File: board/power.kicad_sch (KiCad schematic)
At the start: 2 parts, among them U1 TPS25730D

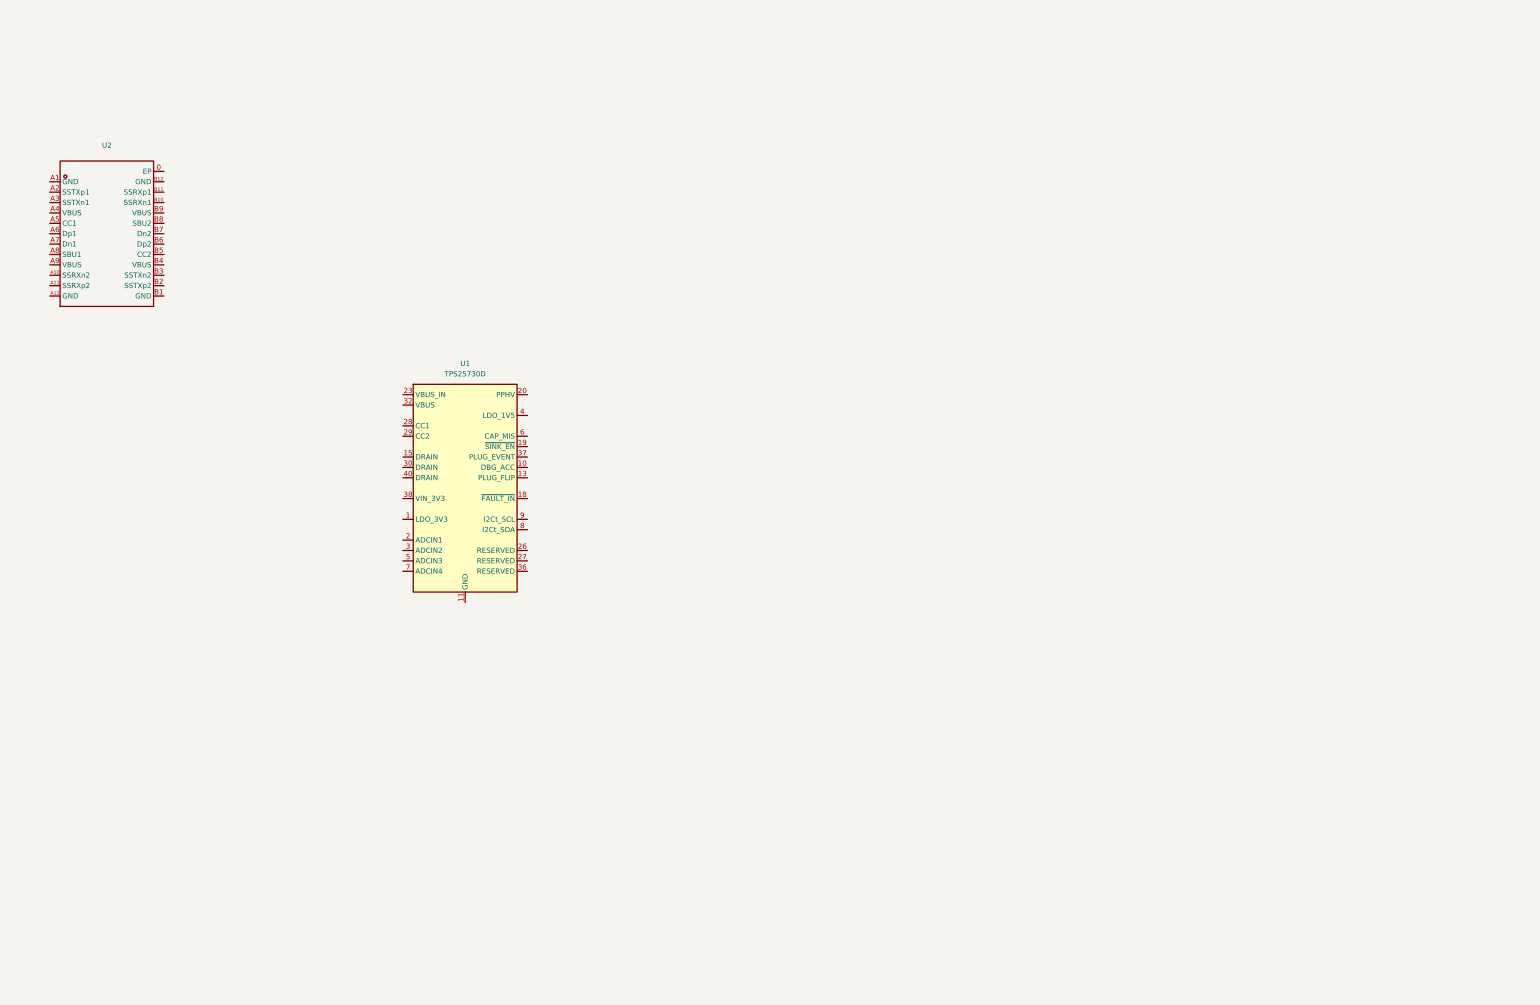
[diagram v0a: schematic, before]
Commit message: Finished everything except assigning footprints for passives
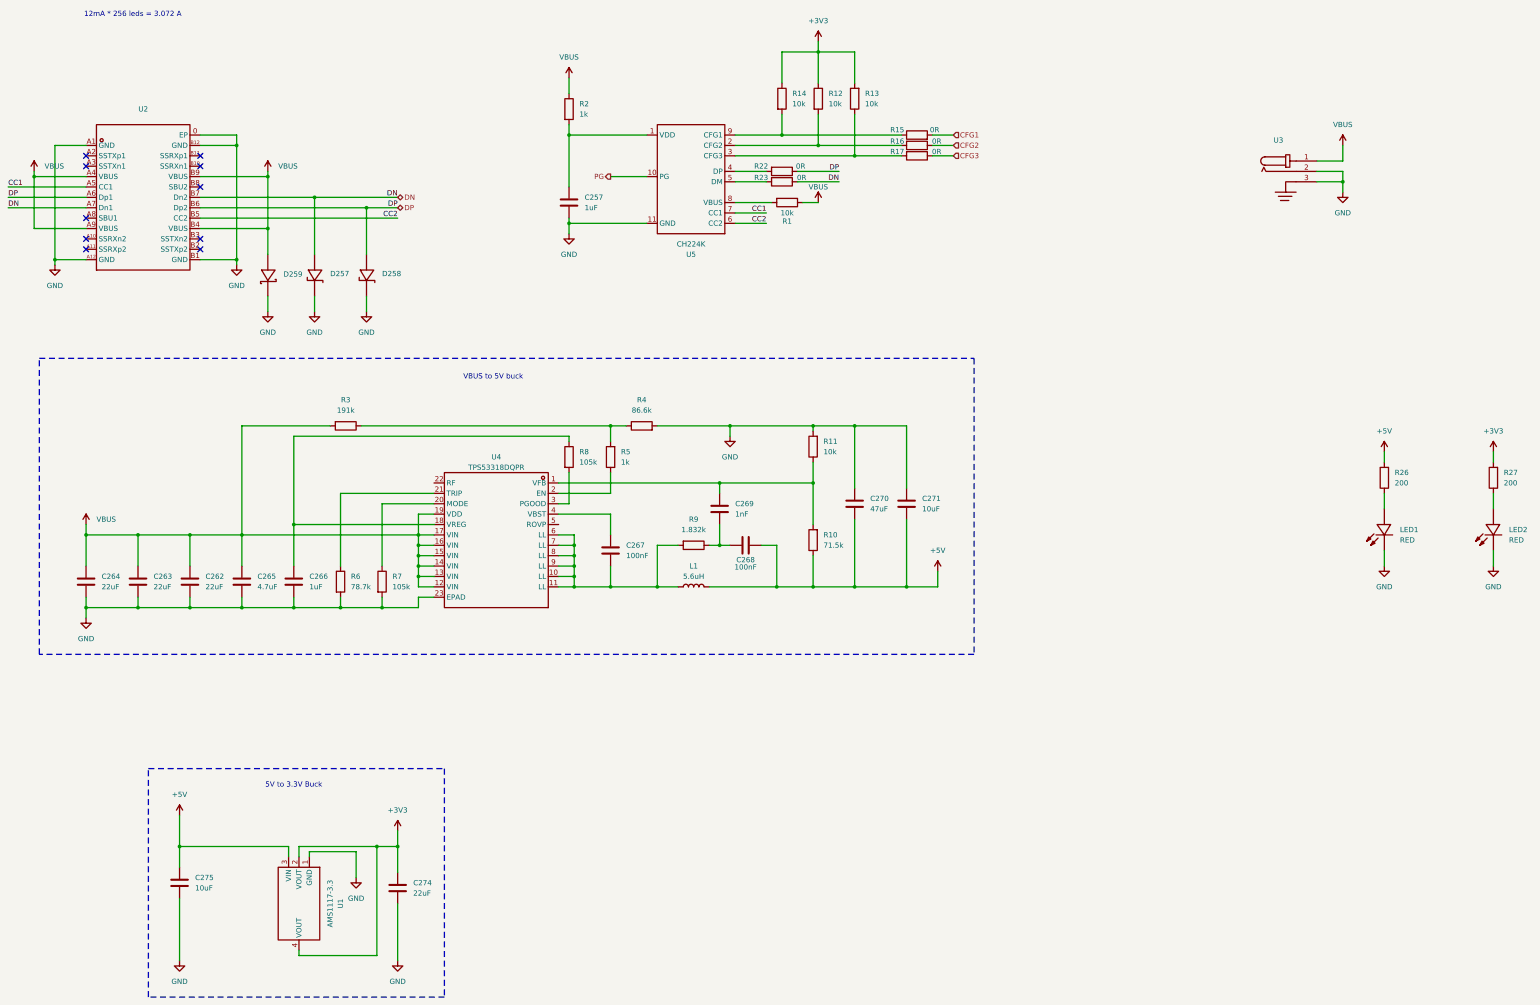
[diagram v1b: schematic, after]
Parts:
- removed U1: TPS25730D, Package_DFN_QFN:Texas_REF0038A_WQFN-38-2EP_6x4mm_P0.4, symbol Interface_USB:TPS25730D
- added C257, C266: 1uF, symbol Device:C
- added C262, C263, C264, C274: 22uF, symbol Device:C
- added C265: 4.7uF, symbol Device:C
- added C267, C268: 100nF, symbol Device:C
- added C269: 1nF, Capacitor_SMD:C_0402_1005Metric_Pad0.74x0.62mm_HandSolder, symbol Device:C
- added C270: 47uF, symbol Device:C
- added C271, C275: 10uF, Capacitor_SMD:C_0402_1005Metric_Pad0.74x0.62mm_HandSolder, symbol Device:C
- added D257, D258: ~, led_matrix:SOD-523F_L1.2-W0.8-LS1.7-RD, symbol led_matrix:ESD5Z5.0T1G
- added D259: ~, led_matrix:SOD-123_L2.7-W1.6-LS3.7-RD, symbol led_matrix:SMF22A
- added L1: 5.6uH, symbol Device:L
- added LED1, LED2: RED, led_matrix:LED0603-RD, symbol led_matrix:KT-0603R
- added R1, R11, R12, R13, R14: 10k, symbol Device:R
- added R10: 71.5k, symbol Device:R
- added R15, R16, R17, R22, R23: 0R, symbol Device:R
- added R2, R5: 1k, symbol Device:R
- added R26, R27: 200, symbol Device:R
- added R3: 191k, symbol Device:R
- added R4: 86.6k, symbol Device:R
- added R6: 78.7k, symbol Device:R
- added R7, R8: 105k, symbol Device:R
- added R9: 1.832k, symbol Device:R
- added U1: AMS1117-3.3, led_matrix:SOT-223-3_L6.5-W3.4-P2.30-LS7.0-BR, symbol led_matrix:AMS1117-3.3
- added U3: ~, led_matrix:DC-IN-TH_HX-DC007B-2.5, symbol led_matrix:HX DC007B-2.5
- added U4: TPS53318DQPR, led_matrix:LSON-CLIP-22_L6.0-W5.0-P0.50-BL-EP, symbol led_matrix:TPS53318DQPR
- added U5: CH224K, led_matrix:ESSOP-10_L4.9-W3.9-P1.0-LS6.0-TL-EP, symbol led_matrix:CH224K
- U2: footprint ProLib_pcs_2025-07-06:TYPE-C-USB-SMD_QCHT-143 -> led_matrix:TYPE-C-USB-SMD_QCHT-143
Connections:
- net GND: now reaches U2.0 (EP)
- net GND: now also U2.A1 (GND), U2.A12 (GND), U2.B1 (GND), U2.B12 (GND), C257.2, C262.2, C263.2, C264.2, C265.2, C266.2, C270.1, C271.1, C274.2, C275.2, D257.1 (C), D258.1 (C), D259.1 (K), LED1.1 (K), LED2.1 (K), R11.2, R4.2, R6.2, R7.2, U1.1 (GND), U3.2, U3.3, U4.23 (EPAD), U5.11 (GND)
- net VBUS: now reaches U2.A4 (VBUS)
- net VBUS: now also U2.A9 (VBUS), U2.B4 (VBUS), U2.B9 (VBUS), C262.1, C263.1, C264.1, C265.1, D259.2 (A), R1.1, R2.1, R3.2, U3.1, U4.12 (VIN), U4.13 (VIN), U4.14 (VIN), U4.15 (VIN), U4.16 (VIN), U4.17 (VIN), U4.19 (VDD)
- net CC1: now reaches U2.A5 (CC1)
- net CC1: now also U5.7 (CC1)
- net DP: now reaches U2.A6 (Dp1)
- net DP: now also U2.B6 (Dp2), D258.2 (A), R22.1
- net DN: now reaches U2.A7 (Dn1)
- net DN: now also U2.B7 (Dn2), D257.2 (A), R23.1
- net CC2: now reaches U2.B5 (CC2)
- net CC2: now also U5.6 (CC2)
- new net: C257.1, R2.2, U5.1 (VDD)
- new net: R13.1, R17.2, U5.3 (CFG3)
- new net: C268.1, C269.1, R9.1
- new net: C267.1, L1.1, R9.2, U4.10 (LL), U4.11 (LL), U4.6 (LL), U4.7 (LL), U4.8 (LL), U4.9 (LL)
- new net: R22.2, U5.4 (DP)
- new net: R3.1, R4.1, R5.2
- new net: C269.2, R10.2, R11.1, U4.1 (VFB)
- new net: R1.2, U5.8 (VBUS)
- new net: R12.2, R16.2, U5.2 (CFG2)
- new net: R23.2, U5.5 (DM)
- new net: R14.2, R15.1, U5.9 (CFG1)
- new net: R7.1, U4.20 (MODE)
- new net: C266.1, R8.1, U4.18 (VREG)
- new net: R8.2, U4.3 (PGOOD)
- new net: R5.1, U4.2 (EN)
- new net: R6.1, U4.21 (TRIP)
- new net: C267.2, U4.4 (VBST)
- new net: LED2.2 (A), R27.1
- new net: LED1.2 (A), R26.1
- new net +3V3: C274.1, R12.1, R13.2, R14.1, R27.2, U1.2 (VOUT), U1.4 (VOUT)
- new net +5V: C268.2, C270.2, C271.2, C275.1, L1.2, R10.1, R26.2, U1.3 (VIN)
- new net CFG1: R15.2
- new net CFG2: R16.1
- new net CFG3: R17.1
- new net PG: U5.10 (PG)
- no-connect marks 0 -> 10
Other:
- note added: "12mA * 256 leds = 3.072 A"
- note added: "5V to 3.3V Buck"
- note added: "VBUS to 5V buck"

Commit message: Added footprints for everything except buck inductor and resistor
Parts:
- C257, C266: footprint (none) -> Capacitor_SMD:C_0402_1005Metric_Pad0.74x0.62mm_HandSolder; LCSC Part Name (none) -> C52923
- C262, C263, C264, C274: footprint (none) -> Capacitor_SMD:C_0805_2012Metric_Pad1.18x1.45mm_HandSolder; LCSC Part Name (none) -> C45783
- C265: footprint (none) -> Capacitor_SMD:C_0603_1608Metric_Pad1.08x0.95mm_HandSolder; LCSC Part Name (none) -> C19666
- C267, C268: footprint (none) -> Capacitor_SMD:C_0402_1005Metric_Pad0.74x0.62mm_HandSolder; LCSC Part Name (none) -> C307331
- C270: footprint (none) -> Capacitor_SMD:C_1206_3216Metric_Pad1.33x1.80mm_HandSolder; LCSC Part Name (none) -> C96123
- R1, R11, R12, R13, R14: footprint (none) -> Resistor_SMD:R_0603_1608Metric_Pad0.98x0.95mm_HandSolder; LCSC Part Name (none) -> C25804
- R10: footprint (none) -> Resistor_SMD:R_0603_1608Metric_Pad0.98x0.95mm_HandSolder; LCSC Part Name (none) -> C304779
- R2, R5: footprint (none) -> Resistor_SMD:R_0402_1005Metric_Pad0.72x0.64mm_HandSolder; LCSC Part Name (none) -> C11702
- R26, R27: footprint (none) -> Resistor_SMD:R_0603_1608Metric_Pad0.98x0.95mm_HandSolder; LCSC Part Name (none) -> C8218
- R3: footprint (none) -> Resistor_SMD:R_0603_1608Metric_Pad0.98x0.95mm_HandSolder; LCSC Part Name (none) -> C2974031
- R4: footprint (none) -> Resistor_SMD:R_0603_1608Metric_Pad0.98x0.95mm_HandSolder; LCSC Part Name (none) -> C304789
- R6: footprint (none) -> Resistor_SMD:R_0603_1608Metric_Pad0.98x0.95mm_HandSolder; LCSC Part Name (none) -> C304782
- R7, R8: footprint (none) -> Resistor_SMD:R_0603_1608Metric_Pad0.98x0.95mm_HandSolder; LCSC Part Name (none) -> C3016070

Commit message: Started layout
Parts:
- removed C270: 47uF, Capacitor_SMD:C_1206_3216Metric_Pad1.33x1.80mm_HandSolder, symbol Device:C
- removed C271: 10uF, Capacitor_SMD:C_0402_1005Metric_Pad0.74x0.62mm_HandSolder, symbol Device:C
- removed D257, D258: ~, led_matrix:SOD-523F_L1.2-W0.8-LS1.7-RD, symbol led_matrix:ESD5Z5.0T1G
- removed D259: ~, led_matrix:SOD-123_L2.7-W1.6-LS3.7-RD, symbol led_matrix:SMF22A
- removed L1: 5.6uH, symbol Device:L
- removed U2: ~, led_matrix:TYPE-C-USB-SMD_QCHT-143, symbol led_matrix:TYPE-C 24P QCHT 143
- removed U3: ~, led_matrix:DC-IN-TH_HX-DC007B-2.5, symbol led_matrix:HX DC007B-2.5
- added C270, C271: 1mF, led_matrix:CAP_EEFC_G_PAN-L, symbol led_matrix:EEE-FC1A102P
- added C276: 22uF, Capacitor_SMD:C_1206_3216Metric_Pad1.33x1.80mm_HandSolder, symbol Device:C
- added C277: 560uF, led_matrix:PCAP_SVP_F12_PAN-L, symbol led_matrix:10SVP560M
- added D257, D258: ~, led_matrix:SOD-523_L1.2-W0.8-LS1.6-BI, symbol led_matrix:LESD5D5.0CT1G
- added DC1: ~, led_matrix:DC-IN-TH_DC-005-5A-2.0-SMT, symbol led_matrix:DC-005-5A-2.5-SMT
- added L1: 4.7uH, led_matrix:IND_BOURNS_SRP1250-L, symbol led_matrix:SRP1250-4R7M
- added USB1: ~, led_matrix:USB-C-SMD_GT-USB-7047A, symbol led_matrix:GT-USB-7047A
- C262, C263, C264, C274: footprint Capacitor_SMD:C_0805_2012Metric_Pad1.18x1.45mm_HandSolder -> Capacitor_SMD:C_1206_3216Metric_Pad1.33x1.80mm_HandSolder; LCSC Part Name C45783 -> C12891
- C265: footprint Capacitor_SMD:C_0603_1608Metric_Pad1.08x0.95mm_HandSolder -> Capacitor_SMD:C_1206_3216Metric_Pad1.33x1.80mm_HandSolder; LCSC Part Name C19666 -> C29823
- C266: footprint Capacitor_SMD:C_0402_1005Metric_Pad0.74x0.62mm_HandSolder -> Capacitor_SMD:C_0805_2012Metric_Pad1.18x1.45mm_HandSolder; LCSC Part Name C52923 -> C28323
- C267, C268: footprint Capacitor_SMD:C_0402_1005Metric_Pad0.74x0.62mm_HandSolder -> Capacitor_SMD:C_0805_2012Metric_Pad1.18x1.45mm_HandSolder; LCSC Part Name C307331 -> C28233
- C269: footprint Capacitor_SMD:C_0402_1005Metric_Pad0.74x0.62mm_HandSolder -> Capacitor_SMD:C_0805_2012Metric_Pad1.18x1.45mm_HandSolder; LCSC Part Name C1523 -> C46653
- C275: footprint Capacitor_SMD:C_0402_1005Metric_Pad0.74x0.62mm_HandSolder -> Capacitor_SMD:C_0603_1608Metric_Pad1.08x0.95mm_HandSolder; LCSC Part Name (none) -> C19702
- LED1, LED2: LCSC Part Name 0603 红灯 高亮 -> C2286
- R15, R16, R17, R22, R23: footprint (none) -> Resistor_SMD:R_0603_1608Metric_Pad0.98x0.95mm_HandSolder; LCSC Part Name (none) -> C15402
- R3: value 191k -> 237k; LCSC Part Name C2974031 -> C22914
- R6: value 78.7k -> 124k; LCSC Part Name C304782 -> C22788
- R9: value 1.832k -> 1.82k; footprint (none) -> Resistor_SMD:R_0603_1608Metric_Pad0.98x0.95mm_HandSolder; LCSC Part Name (none) -> C25958
- U1: LCSC Part Name 输出3.3V 1A -> C6186
- U4: LCSC Part Name 高效8A或14A同步降压转换器 -> C179745
- U5: LCSC Part Name USBPD等多快充协议受电芯片CH224 -> C970725
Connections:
- net +5V: now also C270.1, C271.1, C277.1, L1.1
- net CC1: now also USB1.A5 (CC1)
- net CC2: now also USB1.B5 (CC2)
- net DN: now also D257.1, USB1.A7 (DN1), USB1.B7 (DN2)
- net DP: now also D258.1, USB1.A6 (DP1), USB1.B6 (DP2)
- net GND: now also C270.2, C271.2, C276.2, C277.2, D257.2, D258.2, DC1.2, USB1.1 (SHELL), USB1.2 (SHELL), USB1.3 (SHELL), USB1.4 (SHELL), USB1.A1B12 (GND), USB1.B1A12 (GND)
- net VBUS: now also C276.1, DC1.1, USB1.A4B9 (VBUS), USB1.B4A9 (VBUS)
- net at C267.1, R9.2, U4.10 (LL)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: now also L1.2
- no-connect marks 10 -> 2
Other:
- note added: "5V to 3.3V LDO"
- note added: "A resistor between the inductor and ground is necessary. The value of this resistor is ESR, and can be determined with equation 16. ESR = (L * f_sw) / 60 ESR = 0.0629 Ohms"
- note added: "Maximum current: 256 * 0.012A = 3.072A f_sw = 500kHz From datasheet, inductor ripple current should be from 0.25 to 0.5 times max output current. I have chosen 1/3 ripple current. Inductor ripple current can be used to find inductance value according to the following equation (14): L = (3/(I_out(max) * f_sw)) * (((V_in(max) - Vout) * Vout)/V_in(max)) L = 7.55uH The peak inductor current can be es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"
- note removed: "12mA * 256 leds = 3.072 A"
- note removed: "5V to 3.3V Buck"
- moved on the sheet: LED1, LED2, R26, R27

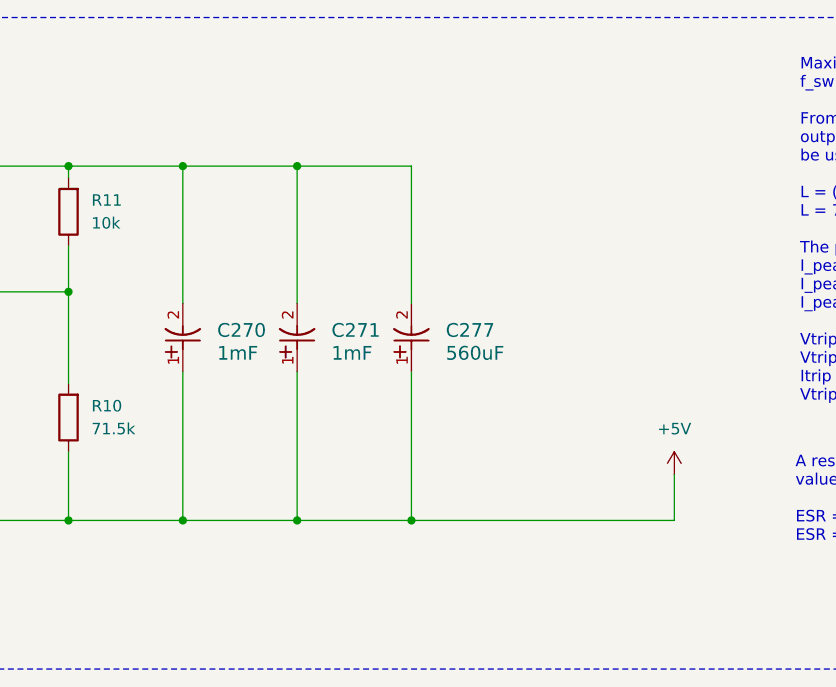
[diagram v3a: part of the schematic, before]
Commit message: Fixed buck output caps
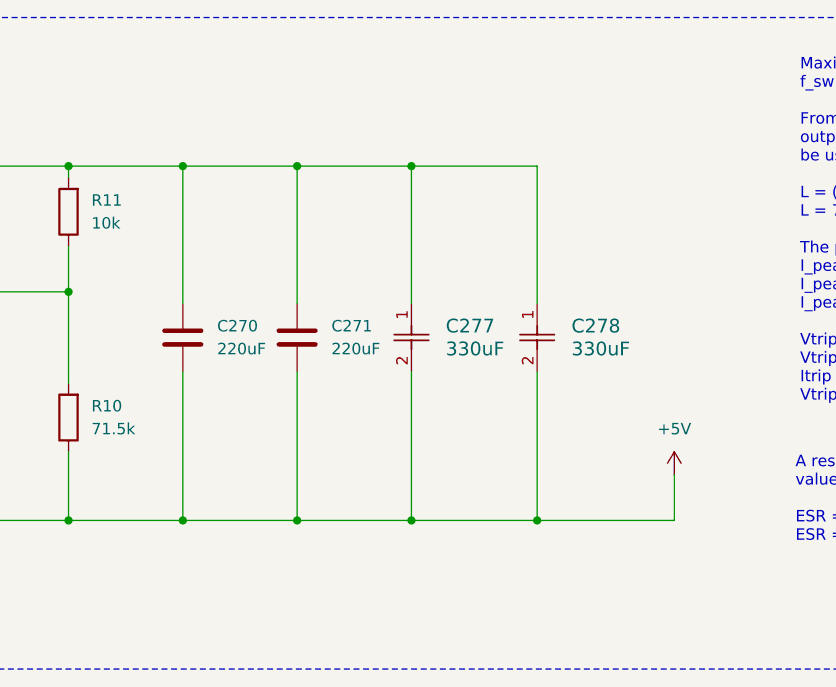
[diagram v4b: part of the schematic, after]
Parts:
- removed C270, C271: 1mF, led_matrix:CAP_EEFC_G_PAN-L, symbol led_matrix:EEE-FC1A102P
- removed C277: 560uF, led_matrix:PCAP_SVP_F12_PAN-L, symbol led_matrix:10SVP560M
- added C270, C271: 220uF, Capacitor_SMD:C_1206_3216Metric_Pad1.33x1.80mm_HandSolder, symbol Device:C
- added C277, C278: 330uF, led_matrix:CAP_293D_E_VIS-L, symbol led_matrix:293D337X9010E2TE3
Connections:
- net +5V: now also C270.2, C271.2, C277.2, C278.2
- net GND: now also C270.1, C271.1, C277.1, C278.1

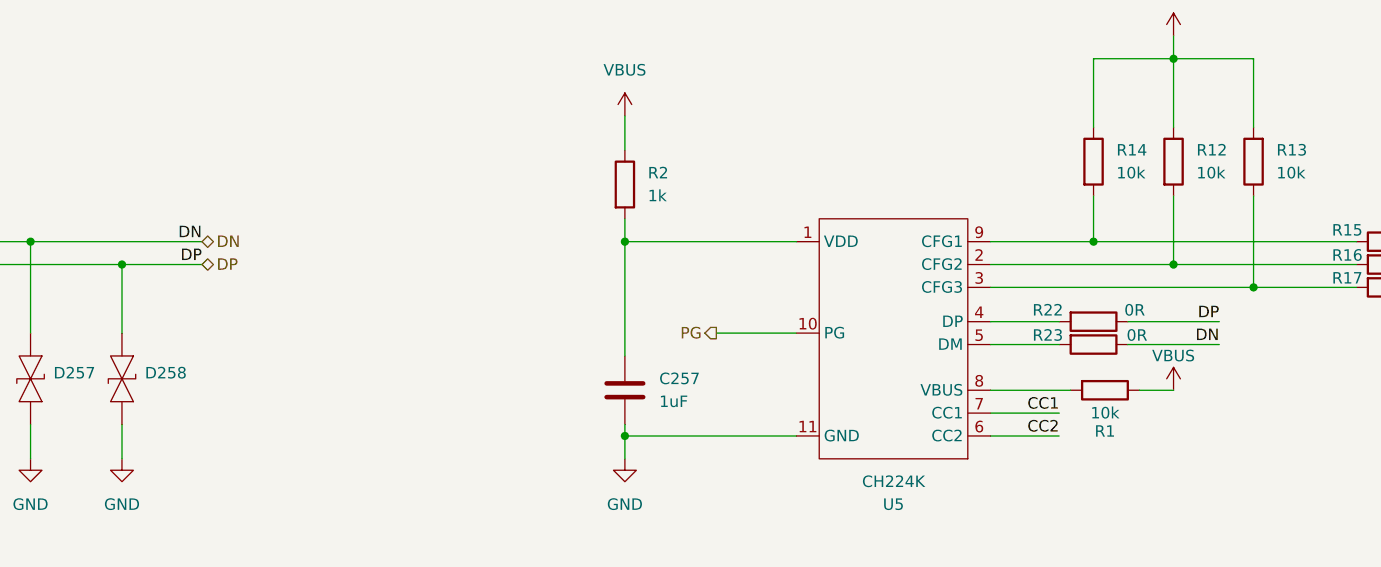
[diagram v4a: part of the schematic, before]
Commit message: Routed usb diff pair
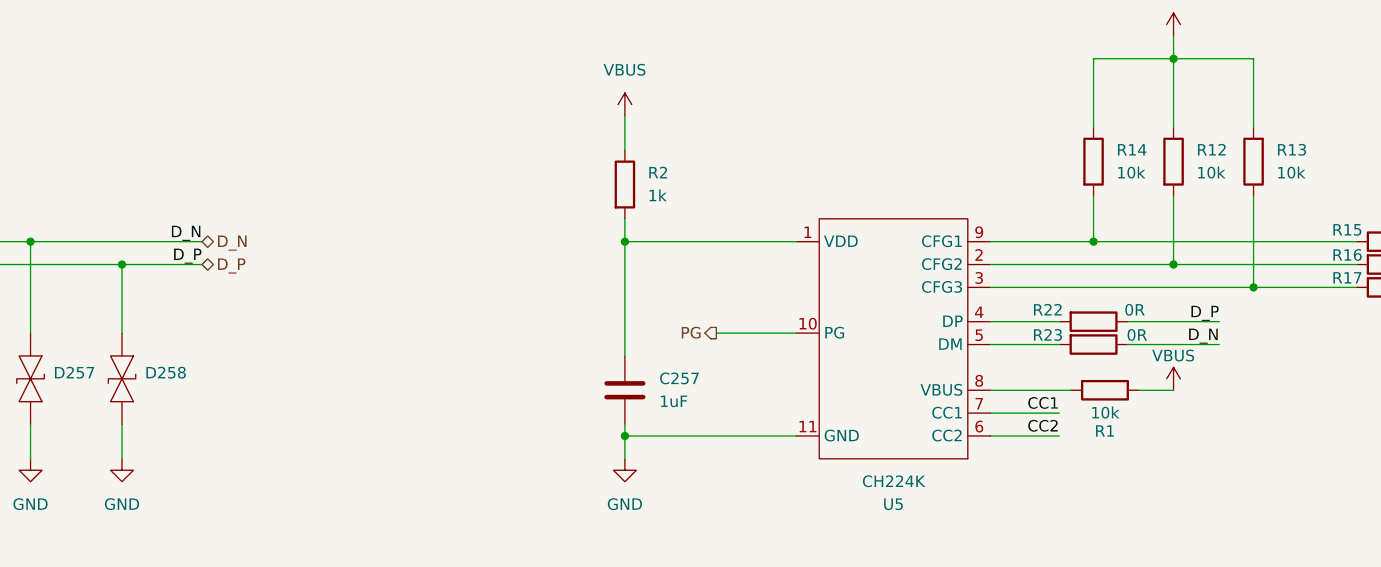
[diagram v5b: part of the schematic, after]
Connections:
- net DN renamed D_N
- net DP renamed D_P
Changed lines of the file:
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@@
 		)
 	)
-	(label "DP"
+	(label "D_P"
 		(at 114.3 58.42 180)
 		(effects
@@
 		)
 	)
-	(label "DN"
+	(label "D_N"
 		(at 114.3 55.88 180)
 		(effects
@@
 		)
 	)
-	(label "DN"
+	(label "D_N"
 		(at 227.33 67.31 180)
 		(effects
@@
 		)
 	)
-	(label "DP"
+	(label "D_P"
 		(at 227.33 64.77 180)
 		(effects
@@
 		)
 	)
-	(hierarchical_label "DP"
+	(hierarchical_label "D_P"
 		(shape bidirectional)
 		(at 114.3 58.42 0)
@@
 		)
 	)
-	(hierarchical_label "DN"
+	(hierarchical_label "D_N"
 		(shape bidirectional)
 		(at 114.3 55.88 0)

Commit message: Abdul ackbar
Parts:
- C275: footprint Capacitor_SMD:C_0603_1608Metric_Pad1.08x0.95mm_HandSolder -> led_matrix:C_0603_1608Metric_Pad1.08x0.95mm_HandSolder
- LED1, LED2: LCSC Part Name C2286 -> 0603 红灯 高亮
- U1: LCSC Part Name C6186 -> 输出3.3V 1A
- U4: LCSC Part Name C179745 -> 高效8A或14A同步降压转换器
- U5: LCSC Part Name C970725 -> USBPD等多快充协议受电芯片CH224

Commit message: Ordered!
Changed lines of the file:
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@@
 		)
 		(property "Value" "10k"
-			(at 214.63 74.93 90)
+			(at 214.63 76.454 90)
 			(effects
 				(font
